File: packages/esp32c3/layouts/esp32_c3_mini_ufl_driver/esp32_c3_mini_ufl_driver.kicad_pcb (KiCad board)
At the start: 2 copper layers, 9 parts

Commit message: Rebuild all
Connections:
- C3 pad 1: output -> output-1
- R2 pad 1: line-11 -> line
- R3 pad 2: output -> output-1
- U1 pad 3: output-1 -> output
- U1 pad 4: output-1 -> output
- U2 pad 12: line-13 -> line-5
- U2 pad 13: line -> line-6
- U2 pad 16: line-12 -> line-8
- U2 pad 18: line-7 -> line-12
- U2 pad 19: line-8 -> line-7
- U2 pad 20: line-2 -> line-9
- U2 pad 21: line-9 -> line-11
- U2 pad 22: line-11 -> line
- U2 pad 23: output-1 -> output
- U2 pad 26: line-10 -> line-2
- U2 pad 30: line-4 -> line-13
- U2 pad 31: line-5 -> line-4
- U2 pad 6: line-6 -> line-10
- U2 pad 8: output -> output-1
- U3 pad 3: output -> output-1
- U3 pad 4: output -> output-1
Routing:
- net output-1: track 1.63 -> 10.1 mm
- net output: track 10.1 -> 1.63 mm
- net line-11: track 5.04 -> 0.00 mm
- net line: track 0.00 -> 5.04 mm
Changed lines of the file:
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@@
     (net 1 "hv")
     (net 2 "ic.footprint.pins[27].net-net")
-    (net 3 "line")
+    (net 3 "line-6")
     (net 4 "ic.footprint.pins[16].net-net")
     (net 5 "ic.footprint.pins[17].net-net")
     (net 6 "line-3")
-    (net 7 "line-11")
-    (net 8 "line-13")
+    (net 7 "line")
+    (net 8 "line-5")
     (net 9 "ic.footprint.pins[60].net-net")
     (net 10 "ic.footprint.pins[33].net-net")
@@
     (net 13 "ic.footprint.pins[8].net-net")
     (net 14 "ic.footprint.pins[21].net-net")
-    (net 15 "line-4")
+    (net 15 "line-13")
     (net 16 "line-1")
     (net 17 "ic.footprint.pins[25].net-net")
-    (net 18 "line-8")
-    (net 19 "line-12")
+    (net 18 "line-7")
+    (net 19 "line-8")
     (net 20 "ic.footprint.pins[26].net-net")
-    (net 21 "line-6")
-    (net 22 "line-2")
-    (net 23 "line-5")
-    (net 24 "output-1")
-    (net 25 "line-7")
-    (net 26 "output")
-    (net 27 "line-9")
-    (net 28 "line-10")
+    (net 21 "line-10")
+    (net 22 "line-9")
+    (net 23 "line-4")
+    (net 24 "output")
+    (net 25 "line-12")
+    (net 26 "output-1")
+    (net 27 "line-11")
+    (net 28 "line-2")
     (net 29 "ic.footprint.pins[6].net-net")
     (net 30 "ic.footprint.pins[1].net-net")
@@
             (size 0.57 0.54)
             (layers "F.Cu" "F.Mask" "F.Paste")
-            (net 26 "output")
+            (net 26 "output-1")
         )
         (embedded_fonts no)
@@
             (size 0.85 0.55)
             (layers "F.Cu" "F.Mask" "F.Paste")
-            (net 21 "line-6")
+            (net 21 "line-10")
         )
         (pad "7" smd rect
@@
             (size 0.85 0.55)
             (layers "F.Cu" "F.Mask" "F.Paste")
-            (net 26 "output")
+            (net 26 "output-1")
         )
         (pad "9" smd rect
@@
             (size 0.85 0.55)
             (layers "F.Cu" "F.Mask" "F.Paste")
-            (net 8 "line-13")
+            (net 8 "line-5")
         )
         (pad "13" smd rect
@@
             (size 0.85 0.55)
             (layers "F.Cu" "F.Mask" "F.Paste")
-            (net 3 "line")
+            (net 3 "line-6")
         )
         (pad "14" smd rect
@@
             (size 0.85 0.55)
             (layers "F.Cu" "F.Mask" "F.Paste")
-            (net 19 "line-12")
+            (net 19 "line-8")
         )
         (pad "17" smd rect
@@
             (size 0.85 0.55)
             (layers "F.Cu" "F.Mask" "F.Paste")
-            (net 25 "line-7")
+            (net 25 "line-12")
         )
         (pad "19" smd rect
@@
             (size 0.85 0.55)
             (layers "F.Cu" "F.Mask" "F.Paste")
-            (net 18 "line-8")
+            (net 18 "line-7")
         )
         (pad "20" smd rect
@@
             (size 0.85 0.55)
             (layers "F.Cu" "F.Mask" "F.Paste")
-            (net 22 "line-2")
+            (net 22 "line-9")
         )
         (pad "21" smd rect
@@
             (size 0.85 0.55)
             (layers "F.Cu" "F.Mask" "F.Paste")
-            (net 27 "line-9")
+            (net 27 "line-11")
         )
         (pad "22" smd rect
@@
             (size 0.85 0.55)
             (layers "F.Cu" "F.Mask" "F.Paste")
-            (net 7 "line-11")
+            (net 7 "line")
         )
         (pad "23" smd rect
@@
             (size 0.85 0.55)
             (layers "F.Cu" "F.Mask" "F.Paste")
-            (net 24 "output-1")
+            (net 24 "output")
         )
         (pad "24" smd rect
@@
             (size 0.85 0.55)
             (layers "F.Cu" "F.Mask" "F.Paste")
-            (net 28 "line-10")
+            (net 28 "line-2")
         )
         (pad "27" smd rect
@@
             (size 0.85 0.55)
             (layers "F.Cu" "F.Mask" "F.Paste")
-            (net 15 "line-4")
+            (net 15 "line-13")
         )
         (pad "31" smd rect
@@
             (size 0.85 0.55)
             (layers "F.Cu" "F.Mask" "F.Paste")
-            (net 23 "line-5")
+            (net 23 "line-4")
         )
         (pad "32" smd rect
@@
             (size 0.79 0.54)
             (layers "F.Cu" "F.Mask" "F.Paste")
-            (net 26 "output")
+            (net 26 "output-1")
         )
         (pad "2" smd rect
@@
             (size 0.57 0.54)
             (layers "F.Cu" "F.Mask" "F.Paste")
-            (net 7 "line-11")
+            (net 7 "line")
         )
         (pad "2" smd rect
@@
             (size 1.05 0.7)
             (layers "F.Cu" "F.Mask" "F.Paste")
-            (net 24 "output-1")
+            (net 24 "output")
         )
         (pad "4" smd rect
@@
             (size 1.05 0.7)
             (layers "F.Cu" "F.Mask" "F.Paste")
-            (net 24 "output-1")
+            (net 24 "output")
         )
         (embedded_fonts no)
@@
             (size 1.05 0.7)
             (layers "F.Cu" "F.Mask" "F.Paste")
-            (net 26 "output")
+            (net 26 "output-1")
         )
         (pad "4" smd rect
@@
             (size 1.05 0.7)
             (layers "F.Cu" "F.Mask" "F.Paste")
-            (net 26 "output")
+            (net 26 "output-1")
         )
         (embedded_fonts no)

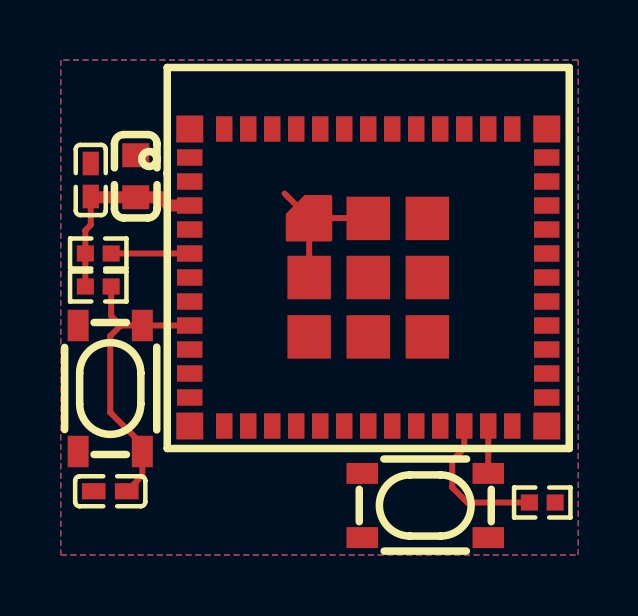
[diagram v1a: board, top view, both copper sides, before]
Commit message: Manually fix fp lib tables
fix some small bugs
fix package only modules (e.g. logos)
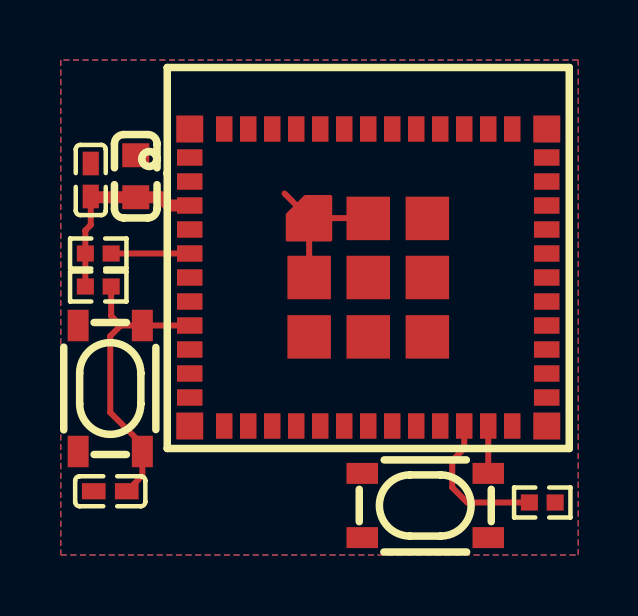
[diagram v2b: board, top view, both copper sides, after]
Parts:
- C1: footprint atopile:C0603-bd72f6 -> Samsung_Electro_Mechanics_CL10A226MQ8NRNC:C0603
- C2: footprint atopile:C0402-b3ef17 -> Samsung_Electro_Mechanics_CL05B104KO5NNNC:C0402
- C3: footprint atopile:C0402-b3ef17 -> Samsung_Electro_Mechanics_CL05A105KA5NQNC:C0402
- R1, R2, R3: footprint atopile:R0402-56259e -> UNI_ROYAL_0402WGF1002TCE:R0402
- U1, U3: footprint lib:KEY-SMD_4P-L4.2-W3.2-P2.20-LS4.6 -> ALPSALPINE_SKRPACE010:KEY-SMD_4P-L4.2-W3.2-P2.20-LS4.6
- U2: footprint atopile:WIFIM-SMD_ESP32-C3-MINI-MINI-1U-1cb675 -> Espressif_Systems_ESP32_C3_MINI_1U_H4:WIFIM-SMD_ESP32-C3-MINI-MINI-1U
- turned U1 to 0 degrees
- turned U3 to -90 degrees
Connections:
- C3 pad 1: output-1 -> line-9
- R2 pad 1: line -> line-5
- R3 pad 2: output-1 -> line-9
- U1 pad 1: gnd -> line-2
- U1 pad 2: gnd -> line-2
- U1 pad 3: output -> gnd
- U1 pad 4: output -> gnd
- U2 pad 12: line-5 -> line
- U2 pad 16: line-8 -> line-11
- U2 pad 18: line-12 -> line-14
- U2 pad 20: line-9 -> line-8
- U2 pad 21: line-11 -> line-4
- U2 pad 22: line -> line-5
- U2 pad 23: output -> line-2
- U2 pad 26: line-2 -> line-10
- U2 pad 27: line-1 -> line-12
- U2 pad 30: line-13 -> line-1
- U2 pad 31: line-4 -> line-13
- U2 pad 6: line-10 -> line-15
- U2 pad 8: output-1 -> line-9
- U3 pad 1: gnd -> line-9
- U3 pad 2: gnd -> line-9
- U3 pad 3: output-1 -> gnd
- U3 pad 4: output-1 -> gnd
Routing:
- net output-1: track 10.1 -> 0.00 mm
- net line-9: track 0.00 -> 10.1 mm
- net line-5: track 0.00 -> 5.04 mm
- net line: track 5.04 -> 0.00 mm
- net output: track 1.63 -> 0.00 mm
- net line-2: track 0.00 -> 1.63 mm

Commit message: Update 3D model locations
fix missing renders
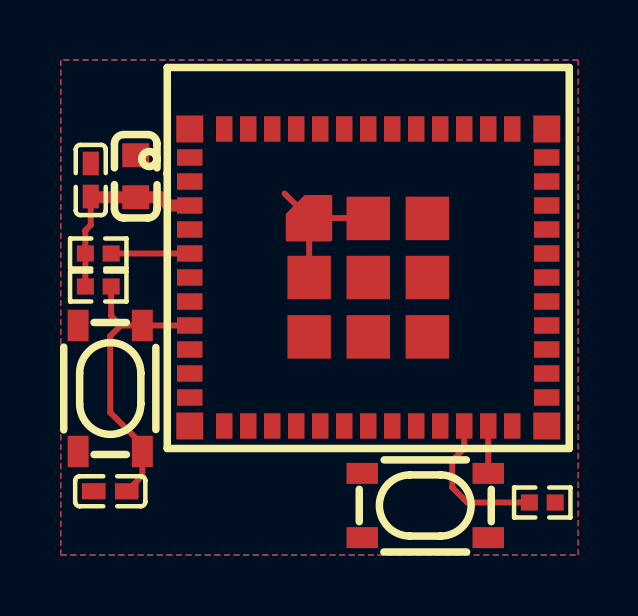
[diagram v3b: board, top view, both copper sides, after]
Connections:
- C3 pad 1: line-9 -> line-7
- R1 pad 1: line-3 -> line-1
- R2 pad 1: line-5 -> line-2
- R3 pad 2: line-9 -> line-7
- U1 pad 1: line-2 -> line-15
- U1 pad 2: line-2 -> line-15
- U2 pad 12: line -> line-3
- U2 pad 13: line-6 -> line-12
- U2 pad 16: line-11 -> line-8
- U2 pad 18: line-14 -> line-6
- U2 pad 19: line-7 -> line
- U2 pad 20: line-8 -> line-13
- U2 pad 21: line-4 -> line-11
- U2 pad 22: line-5 -> line-2
- U2 pad 23: line-2 -> line-15
- U2 pad 26: line-10 -> line-14
- U2 pad 27: line-12 -> line-9
- U2 pad 30: line-1 -> line-10
- U2 pad 31: line-13 -> line-4
- U2 pad 5: line-3 -> line-1
- U2 pad 6: line-15 -> line-5
- U2 pad 8: line-9 -> line-7
- U3 pad 1: line-9 -> line-7
- U3 pad 2: line-9 -> line-7
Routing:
- net line-9: track 10.1 -> 0.00 mm
- net line-7: track 0.00 -> 10.1 mm
- net line-5: track 5.04 -> 0.00 mm
- net line-2: track 1.63 -> 5.04 mm
- net line-3: track 2.67 -> 0.00 mm
- net line-1: track 0.00 -> 2.67 mm
- net line-15: track 0.00 -> 1.63 mm

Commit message: rebuild all packages & regenerate images of changed layouts (silk)
Add new scripts for version bump and build (based on atopile/packages)
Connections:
- C3 pad 1: line-7 -> line-15
- R1 pad 1: line-1 -> line-13
- R2 pad 1: line-2 -> line-7
- R3 pad 2: line-7 -> line-15
- U1 pad 1: line-15 -> line-8
- U1 pad 2: line-15 -> line-8
- U2 pad 12: line-3 -> line
- U2 pad 13: line-12 -> line-1
- U2 pad 16: line-8 -> line-2
- U2 pad 18: line-6 -> line-3
- U2 pad 19: line -> line-4
- U2 pad 20: line-13 -> line-5
- U2 pad 21: line-11 -> line-6
- U2 pad 22: line-2 -> line-7
- U2 pad 23: line-15 -> line-8
- U2 pad 26: line-14 -> line-9
- U2 pad 27: line-9 -> line-10
- U2 pad 30: line-10 -> line-11
- U2 pad 31: line-4 -> line-12
- U2 pad 5: line-1 -> line-13
- U2 pad 6: line-5 -> line-14
- U2 pad 8: line-7 -> line-15
- U3 pad 1: line-7 -> line-15
- U3 pad 2: line-7 -> line-15
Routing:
- net line-15: track 1.63 -> 10.1 mm
- net line-7: track 10.1 -> 5.04 mm
- net line-2: track 5.04 -> 0.00 mm
- net line-13: track 0.00 -> 2.67 mm
- net line-1: track 2.67 -> 0.00 mm
- net line-8: track 0.00 -> 1.63 mm
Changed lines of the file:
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@@
     (net 1 "hv")
     (net 2 "ic.footprint.pins[27].net-net")
-    (net 3 "line-12")
+    (net 3 "line-1")
     (net 4 "ic.footprint.pins[16].net-net")
     (net 5 "ic.footprint.pins[17].net-net")
-    (net 6 "line-1")
-    (net 7 "line-2")
-    (net 8 "line-3")
+    (net 6 "line-13")
+    (net 7 "line-7")
+    (net 8 "line")
     (net 9 "ic.footprint.pins[60].net-net")
     (net 10 "ic.footprint.pins[33].net-net")
@@
     (net 13 "ic.footprint.pins[8].net-net")
     (net 14 "ic.footprint.pins[21].net-net")
-    (net 15 "line-10")
-    (net 16 "line-9")
+    (net 15 "line-11")
+    (net 16 "line-10")
     (net 17 "ic.footprint.pins[25].net-net")
-    (net 18 "line")
-    (net 19 "line-8")
+    (net 18 "line-4")
+    (net 19 "line-2")
     (net 20 "ic.footprint.pins[26].net-net")
-    (net 21 "line-5")
-    (net 22 "line-13")
-    (net 23 "line-4")
-    (net 24 "line-6")
-    (net 25 "line-11")
-    (net 26 "line-14")
+    (net 21 "line-14")
+    (net 22 "line-5")
+    (net 23 "line-12")
+    (net 24 "line-3")
+    (net 25 "line-6")
+    (net 26 "line-9")
     (net 27 "ic.footprint.pins[6].net-net")
     (net 28 "ic.footprint.pins[1].net-net")
     (net 29 "ic.footprint.pins[28].net-net")
     (net 30 "gnd")
-    (net 31 "line-7")
-    (net 32 "line-15")
+    (net 31 "line-15")
+    (net 32 "line-8")
     (footprint "ALPSALPINE_SKRPACE010:KEY-SMD_4P-L4.2-W3.2-P2.20-LS4.6"
         (layer "F.Cu")
@@
             (size 1.05 0.7)
             (layers "F.Cu" "F.Mask" "F.Paste")
-            (net 32 "line-15")
+            (net 32 "line-8")
         )
         (pad "2" smd rect
@@
             (size 1.05 0.7)
             (layers "F.Cu" "F.Mask" "F.Paste")
-            (net 32 "line-15")
+            (net 32 "line-8")
         )
         (pad "3" smd rect
@@
             (size 0.57 0.54)
             (layers "F.Cu" "F.Mask" "F.Paste")
-            (net 6 "line-1")
+            (net 6 "line-13")
         )
         (pad "2" smd rect
@@
             (size 0.57 0.54)
             (layers "F.Cu" "F.Mask" "F.Paste")
-            (net 31 "line-7")
+            (net 31 "line-15")
         )
         (embedded_fonts no)
@@
             (size 0.85 0.55)
             (layers "F.Cu" "F.Mask" "F.Paste")
-            (net 6 "line-1")
+            (net 6 "line-13")
         )
         (pad "6" smd rect
@@
             (size 0.85 0.55)
             (layers "F.Cu" "F.Mask" "F.Paste")
-            (net 21 "line-5")
+            (net 21 "line-14")
         )
         (pad "7" smd rect
@@
             (size 0.85 0.55)
             (layers "F.Cu" "F.Mask" "F.Paste")
-            (net 31 "line-7")
+            (net 31 "line-15")
         )
         (pad "9" smd rect
@@
             (size 0.85 0.55)
             (layers "F.Cu" "F.Mask" "F.Paste")
-            (net 8 "line-3")
+            (net 8 "line")
         )
         (pad "13" smd rect
@@
             (size 0.85 0.55)
             (layers "F.Cu" "F.Mask" "F.Paste")
-            (net 3 "line-12")
+            (net 3 "line-1")
         )
         (pad "14" smd rect
@@
             (size 0.85 0.55)
             (layers "F.Cu" "F.Mask" "F.Paste")
-            (net 19 "line-8")
+            (net 19 "line-2")
         )
         (pad "17" smd rect
@@
             (size 0.85 0.55)
             (layers "F.Cu" "F.Mask" "F.Paste")
-            (net 24 "line-6")
+            (net 24 "line-3")
         )
         (pad "19" smd rect
@@
             (size 0.85 0.55)
             (layers "F.Cu" "F.Mask" "F.Paste")
-            (net 18 "line")
+            (net 18 "line-4")
         )
         (pad "20" smd rect
@@
             (size 0.85 0.55)
             (layers "F.Cu" "F.Mask" "F.Paste")
-            (net 22 "line-13")
+            (net 22 "line-5")
         )
         (pad "21" smd rect
@@
             (size 0.85 0.55)
             (layers "F.Cu" "F.Mask" "F.Paste")
-            (net 25 "line-11")
+            (net 25 "line-6")
         )
         (pad "22" smd rect
@@
             (size 0.85 0.55)
             (layers "F.Cu" "F.Mask" "F.Paste")
-            (net 7 "line-2")
+            (net 7 "line-7")
         )
         (pad "23" smd rect
@@
             (size 0.85 0.55)
             (layers "F.Cu" "F.Mask" "F.Paste")
-            (net 32 "line-15")
+            (net 32 "line-8")
         )
         (pad "24" smd rect
@@
             (size 0.85 0.55)
             (layers "F.Cu" "F.Mask" "F.Paste")
-            (net 26 "line-14")
+            (net 26 "line-9")
         )
         (pad "27" smd rect
@@
             (size 0.85 0.55)
             (layers "F.Cu" "F.Mask" "F.Paste")
-            (net 16 "line-9")
+            (net 16 "line-10")
         )
         (pad "28" smd rect
@@
             (size 0.85 0.55)
             (layers "F.Cu" "F.Mask" "F.Paste")
-            (net 15 "line-10")
+            (net 15 "line-11")
         )
         (pad "31" smd rect
@@
             (size 0.85 0.55)
             (layers "F.Cu" "F.Mask" "F.Paste")
-            (net 23 "line-4")
+            (net 23 "line-12")
         )
         (pad "32" smd rect
@@
             (size 0.79 0.54)
             (layers "F.Cu" "F.Mask" "F.Paste")
-            (net 31 "line-7")
+            (net 31 "line-15")
         )
         (pad "2" smd rect
@@
             (size 0.57 0.54)
             (layers "F.Cu" "F.Mask" "F.Paste")
-            (net 7 "line-2")
+            (net 7 "line-7")
         )
         (pad "2" smd rect
@@
             (size 1.05 0.7)
             (layers "F.Cu" "F.Mask" "F.Paste")
-            (net 31 "line-7")
+            (net 31 "line-15")
         )
         (pad "2" smd rect
@@
             (size 1.05 0.7)
             (layers "F.Cu" "F.Mask" "F.Paste")
-            (net 31 "line-7")
+            (net 31 "line-15")
         )
         (pad "3" smd rect

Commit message: fix(esp32c3): frozen build & unconnected pads
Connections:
- net ic.footprint.pins[16].net-net renamed package.footprint.pins[16].net-net
- net ic.footprint.pins[17].net-net renamed package.footprint.pins[17].net-net
- net ic.footprint.pins[1].net-net renamed package.footprint.pins[1].net-net
- net ic.footprint.pins[20].net-net renamed package.footprint.pins[20].net-net
- net ic.footprint.pins[21].net-net renamed package.footprint.pins[21].net-net
- net ic.footprint.pins[25].net-net renamed package.footprint.pins[25].net-net
- net ic.footprint.pins[26].net-net renamed package.footprint.pins[26].net-net
- net ic.footprint.pins[27].net-net renamed package.footprint.pins[27].net-net
- net ic.footprint.pins[28].net-net renamed package.footprint.pins[28].net-net
- net ic.footprint.pins[33].net-net renamed package.footprint.pins[33].net-net
- net ic.footprint.pins[58].net-net renamed package.footprint.pins[50].net-net
- net ic.footprint.pins[60].net-net renamed package.footprint.pins[52].net-net
- net ic.footprint.pins[6].net-net renamed package.footprint.pins[6].net-net
- net ic.footprint.pins[8].net-net renamed package.footprint.pins[8].net-net
- net line-10 renamed IO19
- net line-13 renamed IO2
- net line-14 renamed IO3
- net line-15 renamed EN
- net line-8 renamed IO9
- net line-9 renamed IO18
- R2 pad 1: line-7 -> line
- U2 pad 12: line -> IO0
- U2 pad 13: line-1 -> IO1
- U2 pad 16: line-2 -> line-1
- U2 pad 18: line-3 -> line-4
- U2 pad 19: line-4 -> line-5
- U2 pad 20: line-5 -> line-6
- U2 pad 21: line-6 -> line-7
- U2 pad 22: line-7 -> line
- U2 pad 30: line-11 -> line-2
- U2 pad 31: line-12 -> line-3
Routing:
- net line-7: track 5.04 -> 0.00 mm
- net line: track 0.00 -> 5.04 mm
